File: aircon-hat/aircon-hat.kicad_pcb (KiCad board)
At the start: 2 copper layers, 54.6 x 40 mm, 17 parts, among them J1 PWM2, J2 Temp: 8, J3 Temp: 7, J4 Temp: 6, J5 Temp: 5, J6 Temp4, J7 Temp3, U1 4N35

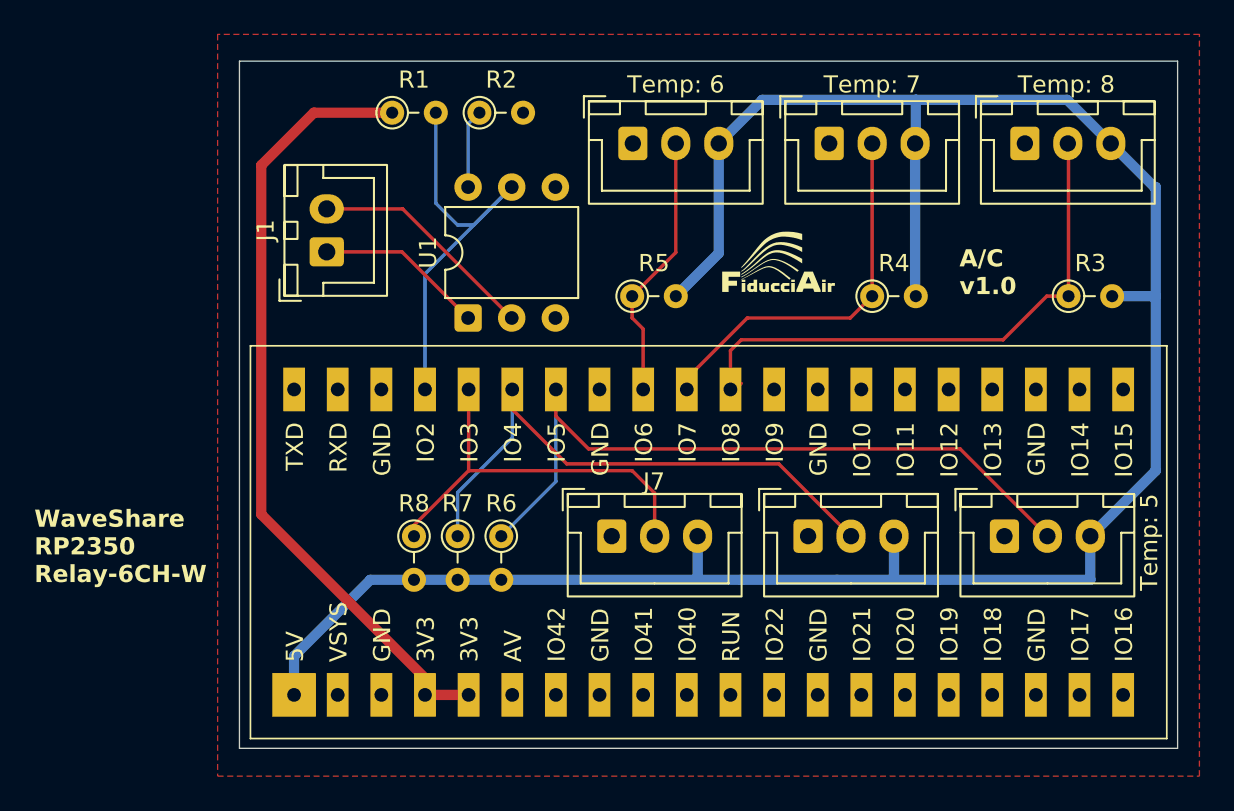
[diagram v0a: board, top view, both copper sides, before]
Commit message: Final aircon hat, handle soft-reset better
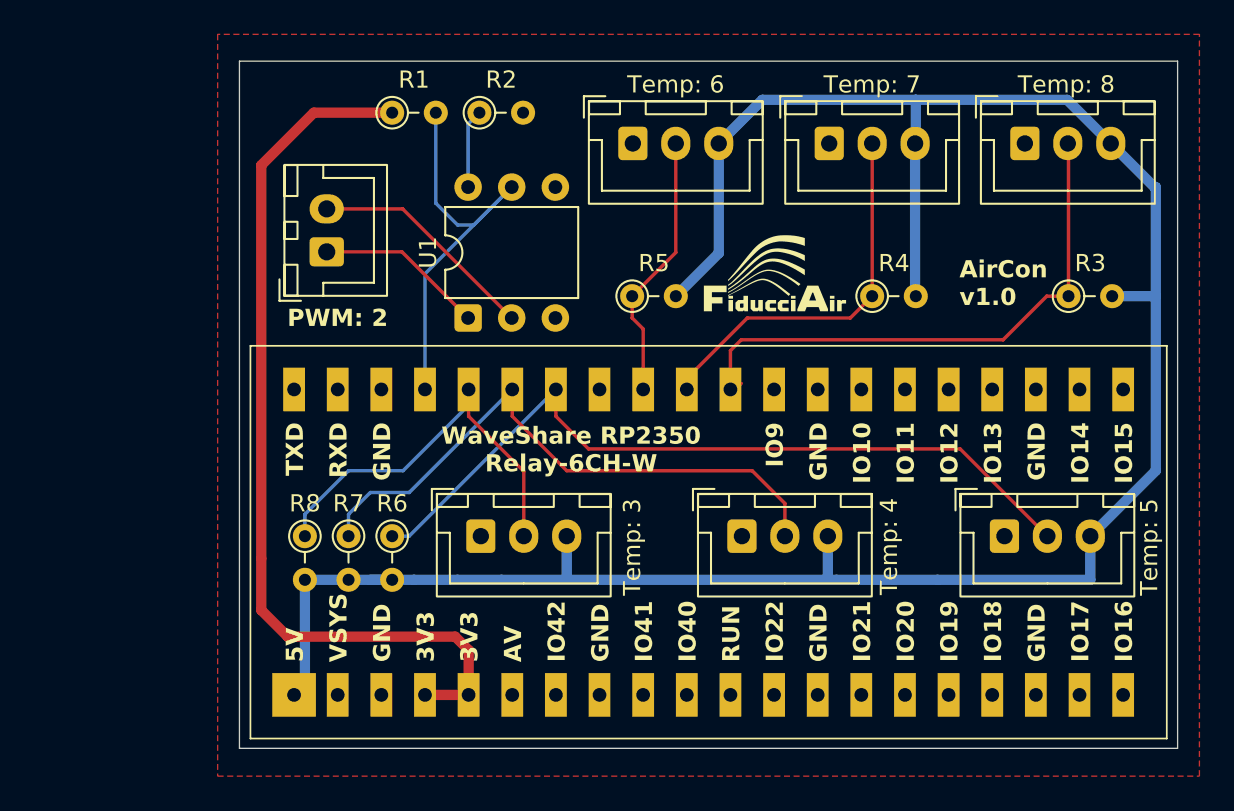
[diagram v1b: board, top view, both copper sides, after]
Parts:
- J1: value PWM2 -> PWM: 2
- J6: value Temp4 -> Temp: 4
- J7: value Temp3 -> Temp: 3
- moved J7 7.62 mm to (73.7, 120.7)
- moved R6 6.35 mm to (68.6, 120.7)
- moved R7 6.35 mm to (66.0, 120.7)
- moved R8 6.35 mm to (63.5, 120.7)
- moved J6 3.85 mm to (88.9, 120.7)
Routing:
- net +3.3V: track 46.2 -> 53.0 mm
- net +5V: track 132.6 -> 136.1 mm
- net Net-(J5-Pin_2): track 42.9 -> 46.1 mm
- net Net-(J6-Pin_2): track 33.8 -> 35.2 mm
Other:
- board text added: "AirCon v1.0"
- board text added: "JLCJLCJLCJLC"
- board text removed: "A/C v1.0"
